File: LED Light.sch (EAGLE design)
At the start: 11 parts, among them J1 AVR_SPI_PRG_6NS, U1 Tiny85-20-SMT

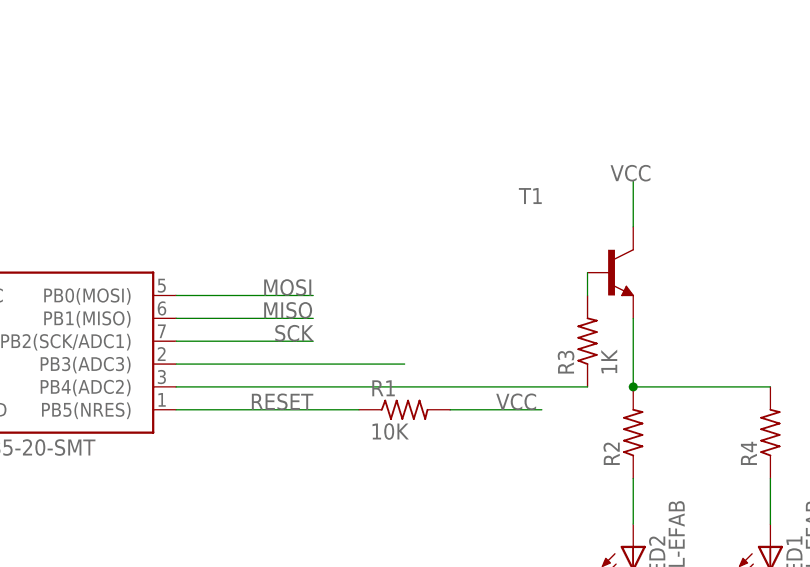
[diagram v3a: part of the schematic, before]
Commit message: Move LEDs to PWM pin (MOSI) and clean up layout.
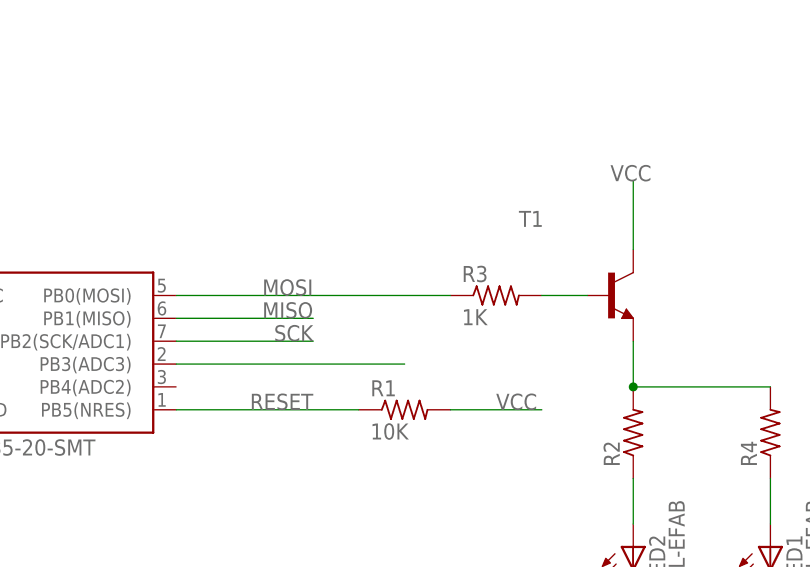
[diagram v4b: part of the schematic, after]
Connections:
- removed net N$4: R3.1, U1.PB4(ADC2)
- net MOSI: now also R3.1
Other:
- moved on the sheet: R3, T1
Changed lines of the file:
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@@
 <instance part="C1" gate="G$1" x="10.16" y="40.64"/>
 <instance part="LED2" gate="G$1" x="91.44" y="15.24"/>
-<instance part="T1" gate="G$1" x="88.9" y="48.26"/>
-<instance part="R3" gate="G$1" x="86.36" y="40.64" rot="R90"/>
+<instance part="T1" gate="G$1" x="88.9" y="45.72"/>
+<instance part="R3" gate="G$1" x="76.2" y="45.72"/>
 <instance part="R4" gate="G$1" x="106.68" y="30.48" rot="R90"/>
 <instance part="LED1" gate="G$1" x="106.68" y="15.24"/>
@@
 <segment>
 <pinref part="T1" gate="G$1" pin="C"/>
-<wire x1="91.44" y1="53.34" x2="91.44" y2="58.42" width="0.1524" layer="91"/>
+<wire x1="91.44" y1="50.8" x2="91.44" y2="58.42" width="0.1524" layer="91"/>
 <label x="88.9" y="58.42" size="1.778" layer="95"/>
 </segment>
@@
 <segment>
 <pinref part="U1" gate="G$1" pin="PB0(MOSI)"/>
-<wire x1="40.64" y1="45.72" x2="55.88" y2="45.72" width="0.1524" layer="91"/>
+<wire x1="40.64" y1="45.72" x2="71.12" y2="45.72" width="0.1524" layer="91"/>
 <label x="55.88" y="45.72" size="1.778" layer="95" rot="MR0"/>
+<pinref part="R3" gate="G$1" pin="1"/>
 </segment>
 </net>
@@
 <pinref part="R2" gate="G$1" pin="2"/>
 <pinref part="T1" gate="G$1" pin="E"/>
-<wire x1="91.44" y1="43.18" x2="91.44" y2="35.56" width="0.1524" layer="91"/>
+<wire x1="91.44" y1="40.64" x2="91.44" y2="35.56" width="0.1524" layer="91"/>
 <pinref part="R4" gate="G$1" pin="2"/>
 <wire x1="91.44" y1="35.56" x2="106.68" y2="35.56" width="0.1524" layer="91"/>
@@
 <pinref part="T1" gate="G$1" pin="B"/>
 <pinref part="R3" gate="G$1" pin="2"/>
-<wire x1="86.36" y1="48.26" x2="86.36" y2="45.72" width="0.1524" layer="91"/>
+<wire x1="86.36" y1="45.72" x2="81.28" y2="45.72" width="0.1524" layer="91"/>
 </segment>
 </net>
-<net name="N$4" class="0">
-<segment>
-<pinref part="U1" gate="G$1" pin="PB4(ADC2)"/>
-<pinref part="R3" gate="G$1" pin="1"/>
-<wire x1="40.64" y1="35.56" x2="86.36" y2="35.56" width="0.1524" layer="91"/>
-</segment>
-</net>

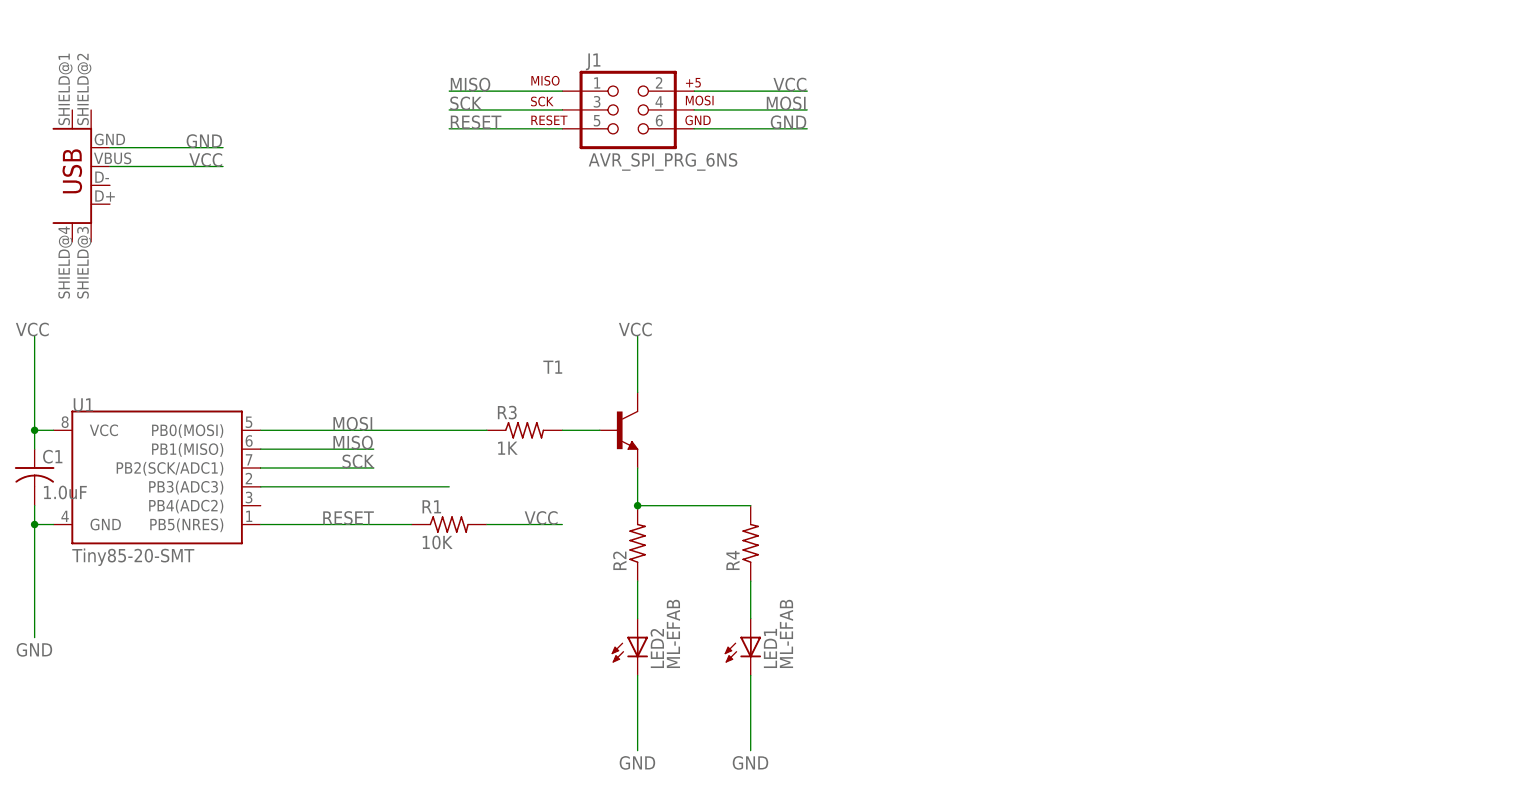
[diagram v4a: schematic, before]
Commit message: Integrate mic into main board, layout in circle.
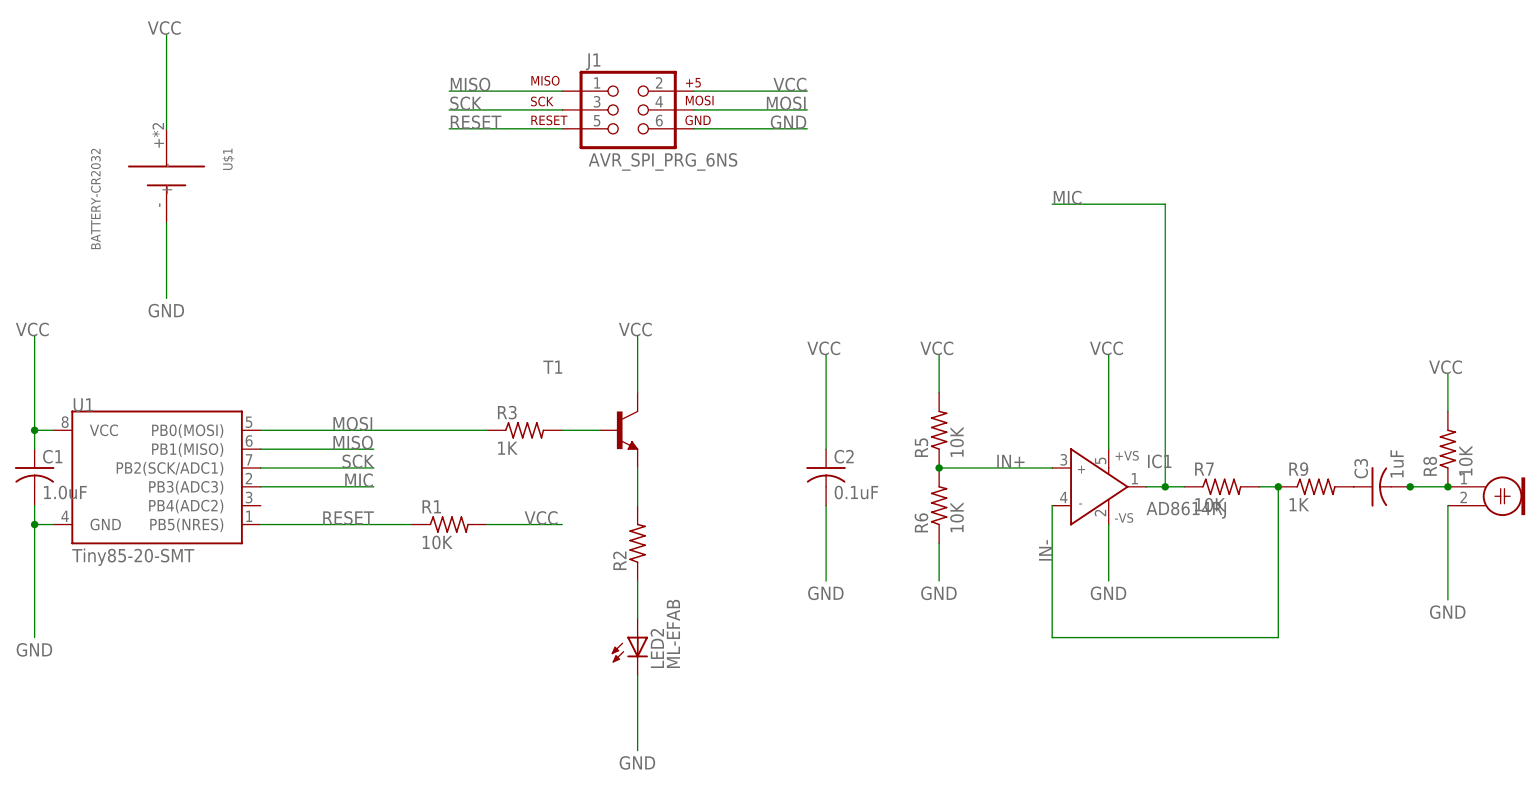
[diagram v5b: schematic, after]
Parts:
- removed JP1: USB_MINIB-POWER, LED Light:USB_MINIB-POWER
- removed LED1: ML-EFAB, LED Light:ML-EFAB
- removed R4: (no value), rcl:R-US_R1206
- added C2: 0.1uF, rcl:C-USC1206
- added C3: 1uF, rcl:C-USC1206
- added IC1: AD8614RJ, analog-devices:AD8614RJ
- added M1: ELECTRET_MICROPHON-WM.64PN, microphon:ELECTRET_MICROPHON-WM.64PN
- added R5, R6, R7, R8: 10K, rcl:R-US_R1206
- added R9: 1K, rcl:R-US_R1206
- added U$1: BATTERY-CR2032, LED Light:BATTERY-CR2032
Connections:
- removed net N$5: LED1G$1.A@1, R4.1
- removed net N$7: U1.PB3(ADC3)
- new net IN+: IC1.IN+, R5.1, R6.2
- new net IN-: IC1.IN-, R7.2, R9.1
- new net MIC: IC1.OUT, R7.1, U1.PB3(ADC3)
- new net N$4: C3.2, M1.1, R8.1
- new net N$6: C3.1, R9.2
- net GND: now also C2.2, IC1.-VS, M1.2, R6.1, U$1.-; no longer JP1.GND, LED1G$1.C@1
- net N$1: no longer R4.2
- net VCC: now also C2.1, IC1.+VS, R5.2, R8.2, U$1.+; no longer JP1.VBUS
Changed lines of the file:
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@@
 <part name="R1" library="rcl" deviceset="R-US_" device="R1206" value="10K"/>
 <part name="R2" library="rcl" deviceset="R-US_" device="R1206"/>
-<part name="JP1" library="LED Light" deviceset="USB_MINIB" device="-POWER"/>
 <part name="C1" library="rcl" deviceset="C-US" device="C1206" value="1.0uF"/>
 <part name="LED2" library="LED Light" deviceset="ML-E" device="FAB"/>
 <part name="T1" library="transistor" deviceset="*-NPN-" device="SOT23-BEC" technology="MMBT3904LT1"/>
 <part name="R3" library="rcl" deviceset="R-US_" device="R1206" value="1K"/>
-<part name="R4" library="rcl" deviceset="R-US_" device="R1206"/>
-<part name="LED1" library="LED Light" deviceset="ML-E" device="FAB"/>
+<part name="IC1" library="analog-devices" deviceset="AD8614" device="RJ"/>
+<part name="R5" library="rcl" deviceset="R-US_" device="R1206" value="10K"/>
+<part name="R6" library="rcl" deviceset="R-US_" device="R1206" value="10K"/>
+<part name="C2" library="rcl" deviceset="C-US" device="C1206" value="0.1uF"/>
+<part name="R7" library="rcl" deviceset="R-US_" device="R1206" value="10K"/>
+<part name="R8" library="rcl" deviceset="R-US_" device="R1206" value="10K"/>
+<part name="C3" library="rcl" deviceset="C-US" device="C1206" value="1uF"/>
+<part name="R9" library="rcl" deviceset="R-US_" device="R1206" value="1K"/>
+<part name="M1" library="microphon" deviceset="ELECTRET_MICROPHON-" device="WM.64PN"/>
+<part name="U$1" library="LED Light" deviceset="BATTERY" device="-CR2032"/>
 </parts>
 <sheets>
@@
 <instance part="R1" gate="G$1" x="66.04" y="33.02"/>
 <instance part="R2" gate="G$1" x="91.44" y="30.48" rot="R90"/>
-<instance part="JP1" gate="G$1" x="17.78" y="78.74" rot="R180"/>
 <instance part="C1" gate="G$1" x="10.16" y="40.64"/>
 <instance part="LED2" gate="G$1" x="91.44" y="15.24"/>
 <instance part="T1" gate="G$1" x="88.9" y="45.72"/>
 <instance part="R3" gate="G$1" x="76.2" y="45.72"/>
-<instance part="R4" gate="G$1" x="106.68" y="30.48" rot="R90"/>
-<instance part="LED1" gate="G$1" x="106.68" y="15.24"/>
+<instance part="IC1" gate="G$1" x="152.4" y="38.1"/>
+<instance part="R5" gate="G$1" x="132.08" y="45.72" rot="R90"/>
+<instance part="R6" gate="G$1" x="132.08" y="35.56" rot="R90"/>
+<instance part="C2" gate="G$1" x="116.84" y="40.64"/>
+<instance part="R7" gate="G$1" x="170.18" y="38.1"/>
+<instance part="R8" gate="G$1" x="200.66" y="43.18" rot="R90"/>
+<instance part="C3" gate="G$1" x="190.5" y="38.1" rot="R90"/>
+<instance part="R9" gate="G$1" x="182.88" y="38.1"/>
+<instance part="M1" gate="G$1" x="205.74" y="38.1"/>
+<instance part="U$1" gate="G$1" x="27.94" y="78.74" rot="R270"/>
 </instances>
 <busses>
@@
 </segment>
 <segment>
-<pinref part="JP1" gate="G$1" pin="VBUS"/>
-<wire x1="20.32" y1="81.28" x2="35.56" y2="81.28" width="0.1524" layer="91"/>
-<label x="35.56" y="81.28" size="1.778" layer="95" rot="MR0"/>
-</segment>
-<segment>
 <pinref part="T1" gate="G$1" pin="C"/>
 <wire x1="91.44" y1="50.8" x2="91.44" y2="58.42" width="0.1524" layer="91"/>
 <label x="88.9" y="58.42" size="1.778" layer="95"/>
+</segment>
+<segment>
+<pinref part="IC1" gate="G$1" pin="+VS"/>
+<wire x1="154.94" y1="43.18" x2="154.94" y2="55.88" width="0.1524" layer="91"/>
+<label x="152.4" y="55.88" size="1.778" layer="95"/>
+</segment>
+<segment>
+<pinref part="R5" gate="G$1" pin="2"/>
+<wire x1="132.08" y1="50.8" x2="132.08" y2="55.88" width="0.1524" layer="91"/>
+<label x="129.54" y="55.88" size="1.778" layer="95"/>
+</segment>
+<segment>
+<wire x1="116.84" y1="43.18" x2="116.84" y2="55.88" width="0.1524" layer="91"/>
+<label x="114.3" y="55.88" size="1.778" layer="95"/>
+<pinref part="C2" gate="G$1" pin="1"/>
+</segment>
+<segment>
+<pinref part="R8" gate="G$1" pin="2"/>
+<wire x1="200.66" y1="48.26" x2="200.66" y2="53.34" width="0.1524" layer="91"/>
+<label x="198.12" y="53.34" size="1.778" layer="95"/>
+</segment>
+<segment>
+<pinref part="U$1" gate="G$1" pin="+"/>
+<wire x1="27.94" y1="86.36" x2="27.94" y2="99.06" width="0.1524" layer="91"/>
+<label x="25.4" y="99.06" size="1.778" layer="95"/>
 </segment>
 </net>
@@
 </segment>
 <segment>
-<pinref part="JP1" gate="G$1" pin="GND"/>
-<wire x1="20.32" y1="83.82" x2="35.56" y2="83.82" width="0.1524" layer="91"/>
-<label x="35.56" y="83.82" size="1.778" layer="95" rot="MR0"/>
-</segment>
-<segment>
 <wire x1="91.44" y1="12.7" x2="91.44" y2="2.54" width="0.1524" layer="91"/>
 <label x="88.9" y="0" size="1.778" layer="95"/>
@@
 </segment>
 <segment>
-<pinref part="LED1" gate="G$1" pin="C@1"/>
-<wire x1="106.68" y1="12.7" x2="106.68" y2="2.54" width="0.1524" layer="91"/>
-<label x="104.14" y="0" size="1.778" layer="95"/>
+<pinref part="IC1" gate="G$1" pin="-VS"/>
+<wire x1="154.94" y1="33.02" x2="154.94" y2="25.4" width="0.1524" layer="91"/>
+<label x="152.4" y="22.86" size="1.778" layer="95"/>
+</segment>
+<segment>
+<pinref part="R6" gate="G$1" pin="1"/>
+<wire x1="132.08" y1="30.48" x2="132.08" y2="25.4" width="0.1524" layer="91"/>
+<label x="129.54" y="22.86" size="1.778" layer="95"/>
+</segment>
+<segment>
+<wire x1="116.84" y1="35.56" x2="116.84" y2="25.4" width="0.1524" layer="91"/>
+<label x="114.3" y="22.86" size="1.778" layer="95"/>
+<pinref part="C2" gate="G$1" pin="2"/>
+</segment>
+<segment>
+<wire x1="200.66" y1="35.56" x2="200.66" y2="22.86" width="0.1524" layer="91"/>
+<label x="198.12" y="20.32" size="1.778" layer="95"/>
+<pinref part="M1" gate="G$1" pin="2"/>
+</segment>
+<segment>
+<pinref part="U$1" gate="G$1" pin="-"/>
+<wire x1="27.94" y1="73.66" x2="27.94" y2="63.5" width="0.1524" layer="91"/>
+<label x="25.4" y="60.96" size="1.778" layer="95"/>
 </segment>
 </net>
@@
 <pinref part="T1" gate="G$1" pin="E"/>
 <wire x1="91.44" y1="40.64" x2="91.44" y2="35.56" width="0.1524" layer="91"/>
-<pinref part="R4" gate="G$1" pin="2"/>
-<wire x1="91.44" y1="35.56" x2="106.68" y2="35.56" width="0.1524" layer="91"/>
-<junction x="91.44" y="35.56"/>
 </segment>
 </net>
@@
 </segment>
 </net>
-<net name="N$5" class="0">
-<segment>
-<pinref part="R4" gate="G$1" pin="1"/>
-<pinref part="LED1" gate="G$1" pin="A@1"/>
-<wire x1="106.68" y1="25.4" x2="106.68" y2="20.32" width="0.1524" layer="91"/>
-</segment>
-</net>
-<net name="N$7" class="0">
+<net name="IN-" class="0">
+<segment>
+<pinref part="R7" gate="G$1" pin="2"/>
+<wire x1="175.26" y1="38.1" x2="177.8" y2="38.1" width="0.1524" layer="91"/>
+<wire x1="177.8" y1="38.1" x2="177.8" y2="17.78" width="0.1524" layer="91"/>
+<wire x1="177.8" y1="17.78" x2="147.32" y2="17.78" width="0.1524" layer="91"/>
+<pinref part="R9" gate="G$1" pin="1"/>
+<junction x="177.8" y="38.1"/>
+<pinref part="IC1" gate="G$1" pin="IN-"/>
+<wire x1="147.32" y1="17.78" x2="147.32" y2="35.56" width="0.1524" layer="91"/>
+<label x="147.32" y="27.94" size="1.778" layer="95" rot="R90"/>
+</segment>
+</net>
+<net name="MIC" class="0">
+<segment>
+<pinref part="IC1" gate="G$1" pin="OUT"/>
+<pinref part="R7" gate="G$1" pin="1"/>
+<wire x1="165.1" y1="38.1" x2="162.56" y2="38.1" width="0.1524" layer="91"/>
+<wire x1="162.56" y1="38.1" x2="160.02" y2="38.1" width="0.1524" layer="91"/>
+<wire x1="162.56" y1="38.1" x2="162.56" y2="76.2" width="0.1524" layer="91"/>
+<junction x="162.56" y="38.1"/>
+<wire x1="162.56" y1="76.2" x2="147.32" y2="76.2" width="0.1524" layer="91"/>
+<label x="147.32" y="76.2" size="1.778" layer="95"/>
+</segment>
 <segment>
 <pinref part="U1" gate="G$1" pin="PB3(ADC3)"/>
-<wire x1="66.04" y1="38.1" x2="40.64" y2="38.1" width="0.1524" layer="91"/>
-</segment>
-</net>
+<wire x1="55.88" y1="38.1" x2="40.64" y2="38.1" width="0.1524" layer="91"/>
+<label x="55.88" y="38.1" size="1.778" layer="95" rot="MR0"/>
+</segment>
+</net>
+<net name="N$4" class="0">
+<segment>
+<pinref part="R8" gate="G$1" pin="1"/>
+<pinref part="C3" gate="G$1" pin="2"/>
+<junction x="195.58" y="38.1"/>
+<pinref part="C3" gate="G$1" pin="2"/>
+<wire x1="195.58" y1="38.1" x2="200.66" y2="38.1" width="0.1524" layer="91"/>
+<pinref part="M1" gate="G$1" pin="1"/>
+<junction x="200.66" y="38.1"/>
+</segment>
+</net>
+<net name="N$6" class="0">
+<segment>
+<pinref part="C3" gate="G$1" pin="1"/>
+<pinref part="R9" gate="G$1" pin="2"/>
+</segment>
+</net>
+<net name="IN+" class="0">
+<segment>
+<pinref part="IC1" gate="G$1" pin="IN+"/>
+<pinref part="R5" gate="G$1" pin="1"/>
+<wire x1="132.08" y1="40.64" x2="147.32" y2="40.64" width="0.1524" layer="91"/>
+<pinref part="R6" gate="G$1" pin="2"/>
+<junction x="132.08" y="40.64"/>
+<label x="139.7" y="40.64" size="1.778" layer="95"/>
+</segment>
+</net>

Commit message: Tweaks to board layout and mic footprint.
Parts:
- M1: value ELECTRET_MICROPHON-WM.64PN -> ELECTRETTH; device microphon:ELECTRET_MICROPHON-WM.64PN -> LED Light:ELECTRETTH
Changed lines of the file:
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@@
 <part name="C3" library="rcl" deviceset="C-US" device="C1206" value="1uF"/>
 <part name="R9" library="rcl" deviceset="R-US_" device="R1206" value="1K"/>
-<part name="M1" library="microphon" deviceset="ELECTRET_MICROPHON-" device="WM.64PN"/>
+<part name="M1" library="LED Light" deviceset="ELECTRET" device="TH"/>
 <part name="U$1" library="LED Light" deviceset="BATTERY" device="-CR2032"/>
 </parts>
@@
 <instance part="C3" gate="G$1" x="190.5" y="38.1" rot="R90"/>
 <instance part="R9" gate="G$1" x="182.88" y="38.1"/>
-<instance part="M1" gate="G$1" x="205.74" y="38.1"/>
+<instance part="M1" gate="G$1" x="208.28" y="38.1"/>
 <instance part="U$1" gate="G$1" x="27.94" y="78.74" rot="R270"/>
 </instances>

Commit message: Add holes; re-route; generate gerbers.
For two-layer board.
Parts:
- IC1: value AD8614RJ -> AD8615AUJZ
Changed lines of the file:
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@@
 <?xml version="1.0" encoding="utf-8"?>
 <!DOCTYPE eagle SYSTEM "eagle.dtd">
-<eagle version="6.5.0">
+<eagle version="6.6.0">
 <drawing>
 <settings>
@@
 <part name="T1" library="transistor" deviceset="*-NPN-" device="SOT23-BEC" technology="MMBT3904LT1"/>
 <part name="R3" library="rcl" deviceset="R-US_" device="R1206" value="1K"/>
-<part name="IC1" library="analog-devices" deviceset="AD8614" device="RJ"/>
+<part name="IC1" library="analog-devices" deviceset="AD8614" device="RJ" value="AD8615AUJZ"/>
 <part name="R5" library="rcl" deviceset="R-US_" device="R1206" value="10K"/>
 <part name="R6" library="rcl" deviceset="R-US_" device="R1206" value="10K"/>

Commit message: Move drills holes and silk; new gerbers.
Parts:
- R2: value (none) -> 24
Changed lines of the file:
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@@
 <part name="J1" library="SparkFun-Connectors" deviceset="AVR_SPI_PRG_6" device="NS"/>
 <part name="R1" library="rcl" deviceset="R-US_" device="R1206" value="10K"/>
-<part name="R2" library="rcl" deviceset="R-US_" device="R1206"/>
+<part name="R2" library="rcl" deviceset="R-US_" device="R1206" value="24"/>
 <part name="C1" library="rcl" deviceset="C-US" device="C1206" value="1.0uF"/>
 <part name="LED2" library="LED Light" deviceset="ML-E" device="FAB"/>
